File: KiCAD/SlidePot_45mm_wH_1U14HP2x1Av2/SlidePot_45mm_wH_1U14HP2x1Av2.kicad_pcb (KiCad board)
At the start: 2 copper layers, 70.8 x 39.7 mm, 7 parts

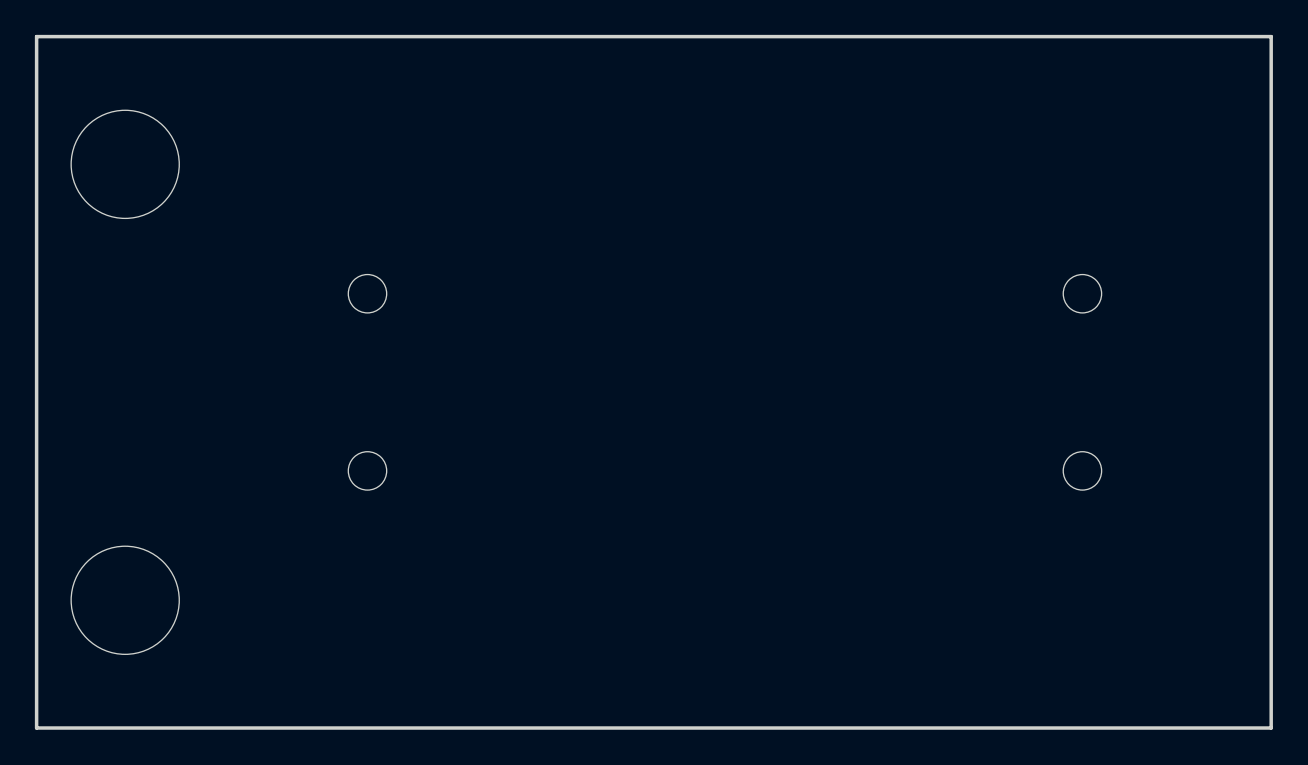
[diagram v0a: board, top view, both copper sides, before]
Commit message: updated all modules to use plated through-holes wherever possible
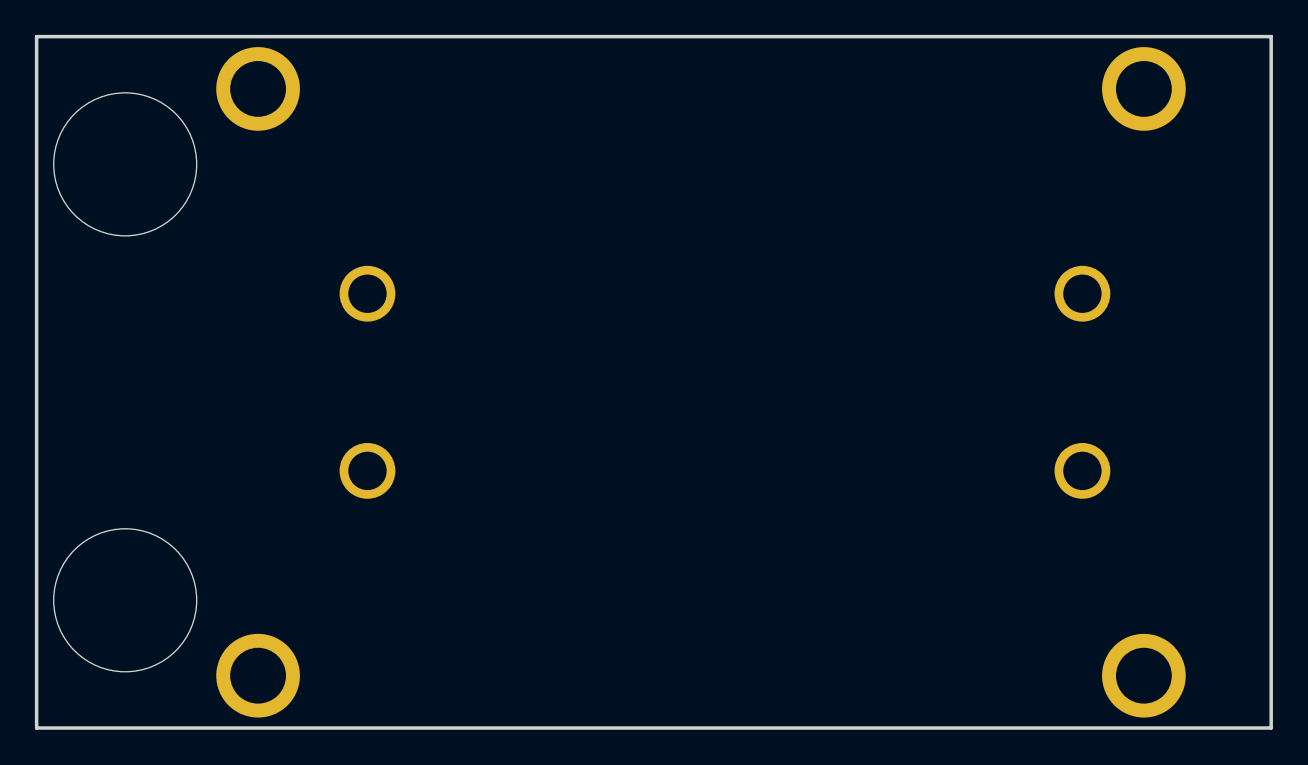
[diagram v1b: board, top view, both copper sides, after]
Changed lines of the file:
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@@
 			)
 		)
-		(pad "" np_thru_hole oval
+		(pad "" thru_hole circle
 			(at 0 0)
-			(size 4.34 3.2)
-			(drill oval 4.34 3.2)
-			(layers "*.Cu" "*.Mask")
+			(size 4.8 4.8)
+			(drill 3.2)
+			(layers "*.Cu" "*.Mask")
+			(remove_unused_layers no)
 		)
 		(embedded_fonts no)
@@
 			)
 		)
-		(pad "" np_thru_hole circle
+		(pad "" thru_hole circle
 			(at 0 -20.5 90)
-			(size 2.2 2.2)
+			(size 3.2 3.2)
 			(drill 2.2)
 			(layers "*.Cu" "*.Mask")
+			(remove_unused_layers no)
 		)
 		(pad "" np_thru_hole oval
@@
 			(layers "*.Cu" "*.Mask")
 		)
-		(pad "" np_thru_hole circle
+		(pad "" thru_hole circle
 			(at 0 20.5 90)
-			(size 2.2 2.2)
+			(size 3.2 3.2)
 			(drill 2.2)
 			(layers "*.Cu" "*.Mask")
+			(remove_unused_layers no)
 		)
 		(embedded_fonts no)
@@
 		(at 5.08 9.75)
 		(property "Reference" "H5"
-			(at 0 -4 0)
+			(at 0 -5 0)
 			(unlocked yes)
 			(layer "B.SilkS")
@@
 		(fp_circle
 			(center 0 0)
-			(end 3.1 0)
+			(end 4.1 0)
 			(stroke
 				(width 0.2)
@@
 		(fp_circle
 			(center 0 25)
-			(end 3.1 25)
+			(end 4.1 25)
 			(stroke
 				(width 0.2)
@@
 		(pad "" np_thru_hole circle
 			(at 0 0)
-			(size 6.2 6.2)
-			(drill 6.2)
+			(size 8.2 8.2)
+			(drill 8.2)
 			(layers "*.Cu" "*.Mask")
 		)
 		(pad "" np_thru_hole circle
 			(at 0 25)
-			(size 6.2 6.2)
-			(drill 6.2)
+			(size 8.2 8.2)
+			(drill 8.2)
 			(layers "*.Cu" "*.Mask")
 		)
@@
 			)
 		)
-		(pad "" np_thru_hole oval
+		(pad "" thru_hole circle
 			(at 0 0)
-			(size 4.34 3.2)
-			(drill oval 4.34 3.2)
-			(layers "*.Cu" "*.Mask")
+			(size 4.8 4.8)
+			(drill 3.2)
+			(layers "*.Cu" "*.Mask")
+			(remove_unused_layers no)
 		)
 		(embedded_fonts no)
@@
 			)
 		)
-		(pad "" np_thru_hole circle
+		(pad "" thru_hole circle
 			(at 0 -20.5 90)
-			(size 2.2 2.2)
+			(size 3.2 3.2)
 			(drill 2.2)
 			(layers "*.Cu" "*.Mask")
+			(remove_unused_layers no)
 		)
 		(pad "" np_thru_hole oval
@@
 			(layers "*.Cu" "*.Mask")
 		)
-		(pad "" np_thru_hole circle
+		(pad "" thru_hole circle
 			(at 0 20.5 90)
-			(size 2.2 2.2)
+			(size 3.2 3.2)
 			(drill 2.2)
 			(layers "*.Cu" "*.Mask")
+			(remove_unused_layers no)
 		)
 		(embedded_fonts no)
@@
 			)
 		)
-		(pad "" np_thru_hole oval
+		(pad "" thru_hole circle
 			(at 0 0)
-			(size 4.34 3.2)
-			(drill oval 4.34 3.2)
-			(layers "*.Cu" "*.Mask")
+			(size 4.8 4.8)
+			(drill 3.2)
+			(layers "*.Cu" "*.Mask")
+			(remove_unused_layers no)
 		)
 		(embedded_fonts no)
@@
 			)
 		)
-		(pad "" np_thru_hole oval
+		(pad "" thru_hole circle
 			(at 0 0)
-			(size 4.34 3.2)
-			(drill oval 4.34 3.2)
-			(layers "*.Cu" "*.Mask")
+			(size 4.8 4.8)
+			(drill 3.2)
+			(layers "*.Cu" "*.Mask")
+			(remove_unused_layers no)
 		)
 		(embedded_fonts no)
